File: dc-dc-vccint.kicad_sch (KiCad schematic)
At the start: 62 parts, among them U36 MP8796B, U4 MP8796B

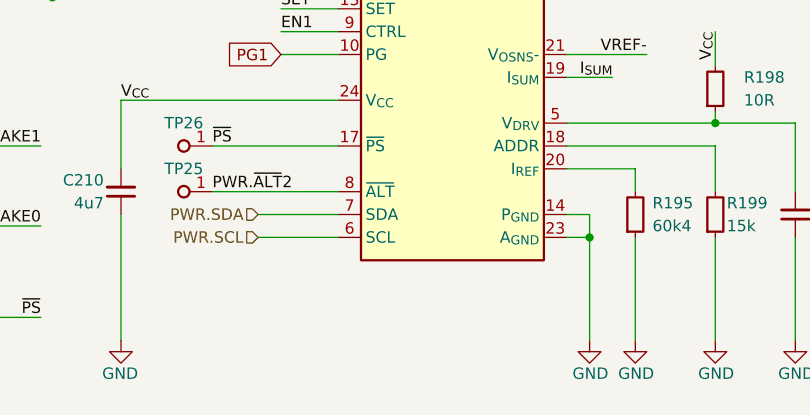
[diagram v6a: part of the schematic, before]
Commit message: [#69798] Fix I2C adresses descriptions on the schematic
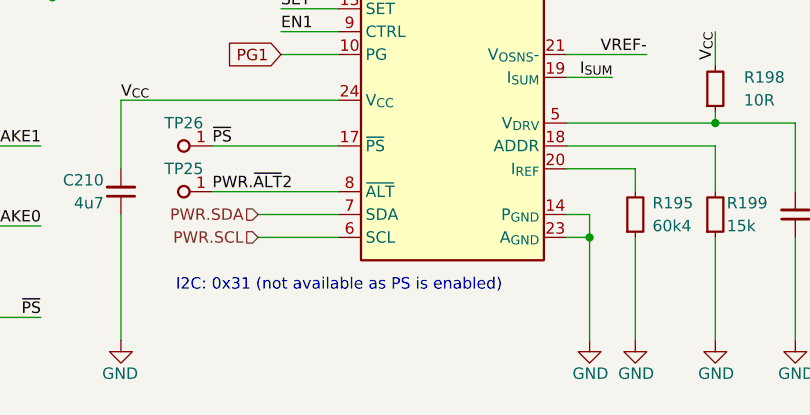
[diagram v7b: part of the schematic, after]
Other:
- note added: "I2C: 0x31 (not available as PS is enabled)"
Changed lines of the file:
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@@
+		)
+	)
+	(text "I2C: 0x31 (not available as PS is enabled)"
+		(exclude_from_sim no)
+		(at 115.316 241.046 0)
+		(effects
+			(font
+				(size 1.27 1.27)
+			)
+			(justify left bottom)
 		)
 	)
